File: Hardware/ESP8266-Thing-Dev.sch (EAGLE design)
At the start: 68 parts, among them J1 DNP, Q1 MMBT2222A, Q2 MMBT2222A, U1 AP2112K-3.3V, U2 ESP8266, U3 AT25SF041-SOIC8, U4 FTS31XS-U, Y1 26MHz

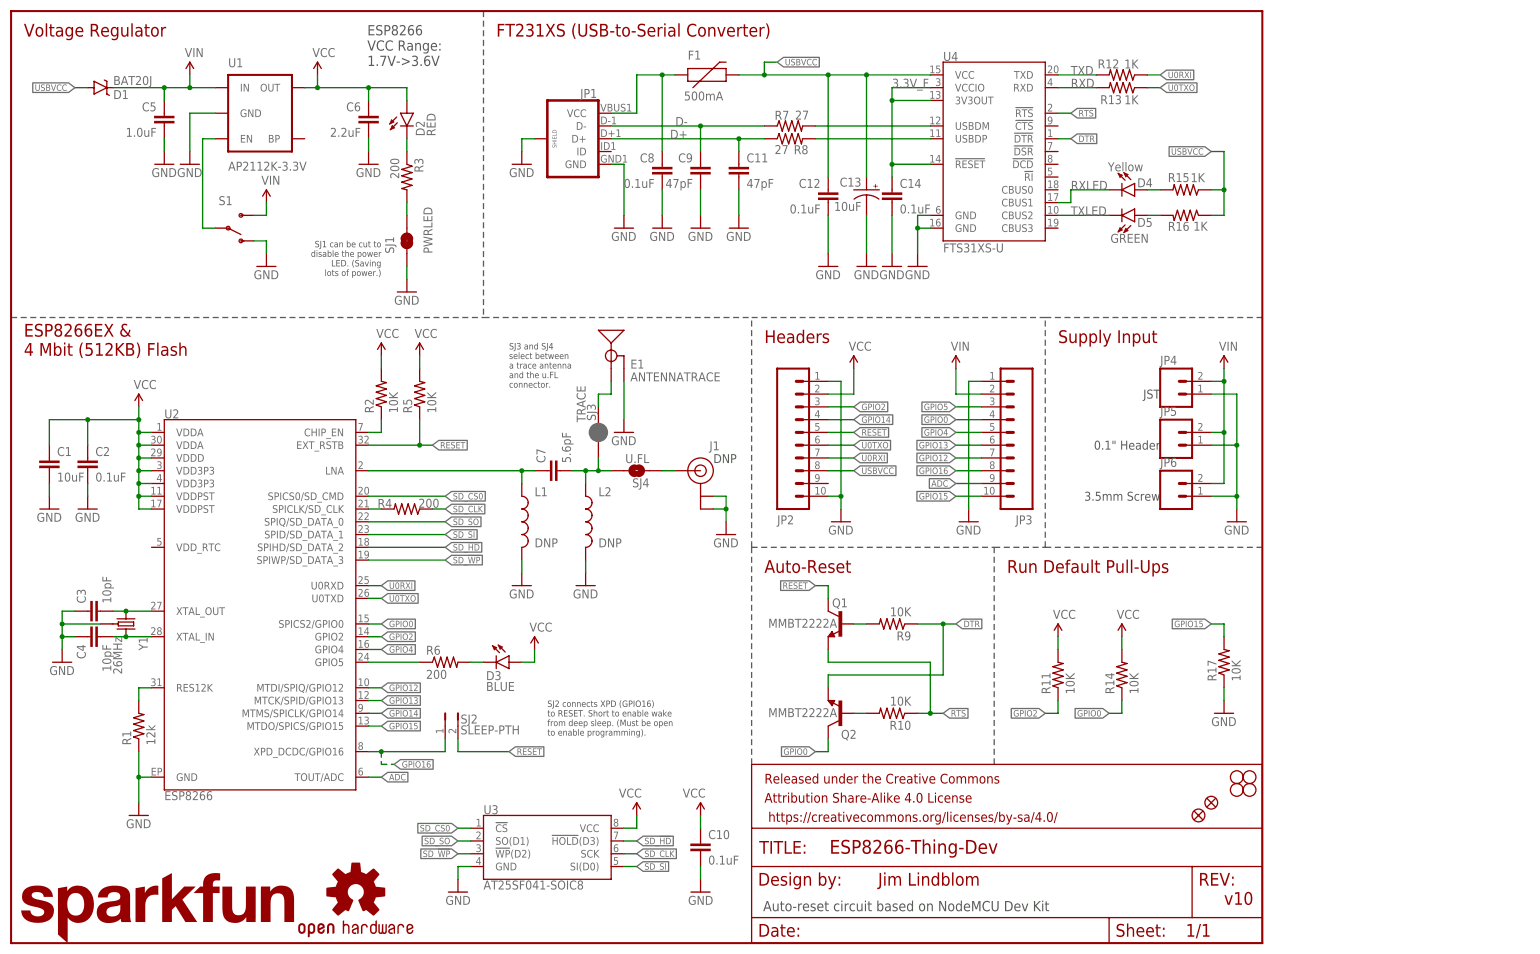
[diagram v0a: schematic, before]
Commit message: Import project and add level shifters in schematic.
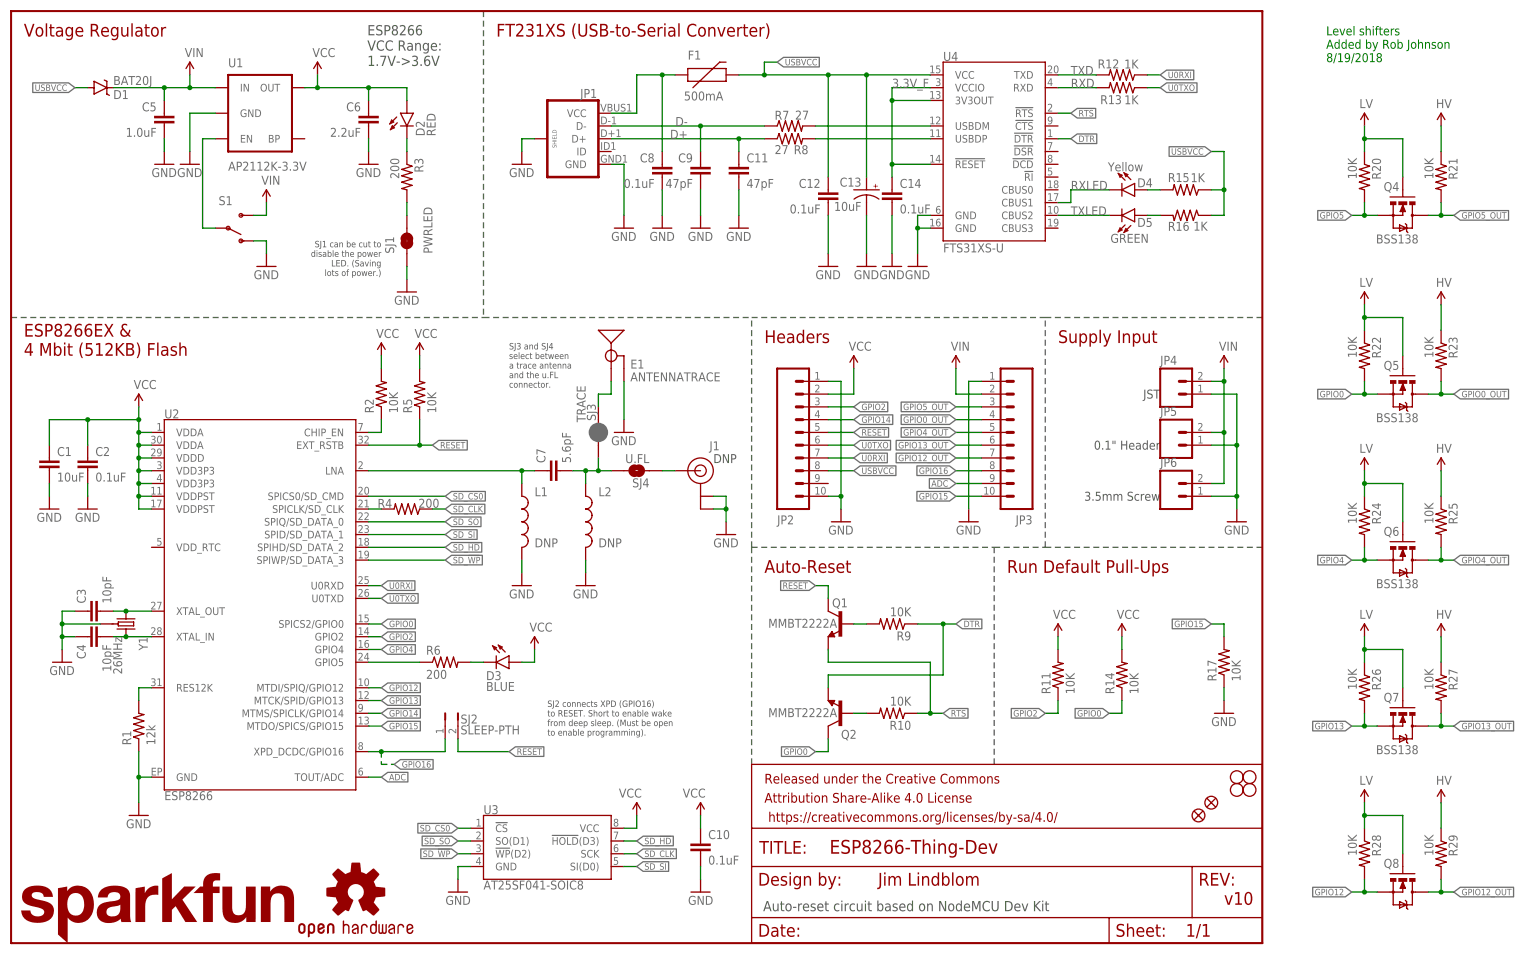
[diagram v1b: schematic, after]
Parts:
- added Q4, Q5, Q6, Q7, Q8: BSS138, SparkFun:MOSFET-NCHANNELSMD
- added R20, R21, R22, R23, R24, R25, R26, R27, R28, R29: 10K, SparkFun:RESISTOR0603-RES
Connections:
- new net GPIO0_OUT: JP3.4, Q5.D, R23.2
- new net GPIO12_OUT: JP3.7, Q8.D, R29.2
- new net GPIO13_OUT: JP3.6, Q7.D, R27.2
- new net GPIO4_OUT: JP3.5, Q6.D, R25.2
- new net GPIO5_OUT: JP3.3, Q4.D, R21.2
- new net HV: R21.1, R23.1, R25.1, R27.1, R29.1
- new net LV: Q5.G, Q6.G, Q7.G, Q8.G, R22.1, R24.1, R26.1, R28.1
- net GPIO0: now also Q5.S, R22.2; no longer JP3.4
- net GPIO12: now also Q8.S, R28.2; no longer JP3.7
- net GPIO13: now also Q7.S, R26.2; no longer JP3.6
- net GPIO4: now also Q6.S, R24.2; no longer JP3.5
- net GPIO5: now also Q4.S, R20.2; no longer JP3.3
- net VCC: now also Q4.G, R20.1
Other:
- note added: "Level shifters Added by Rob Johnson 8/19/2018"

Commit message: Fix Net names for level shifter supply voltages
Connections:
- removed net HV: R21.1, R23.1, R25.1, R27.1, R29.1
- removed net LV: Q5.G, Q6.G, Q7.G, Q8.G, R22.1, R24.1, R26.1, R28.1
- net VCC: now also Q5.G, Q6.G, Q7.G, Q8.G, R22.1, R24.1, R26.1, R28.1
- net VIN: now also R21.1, R23.1, R25.1, R27.1, R29.1

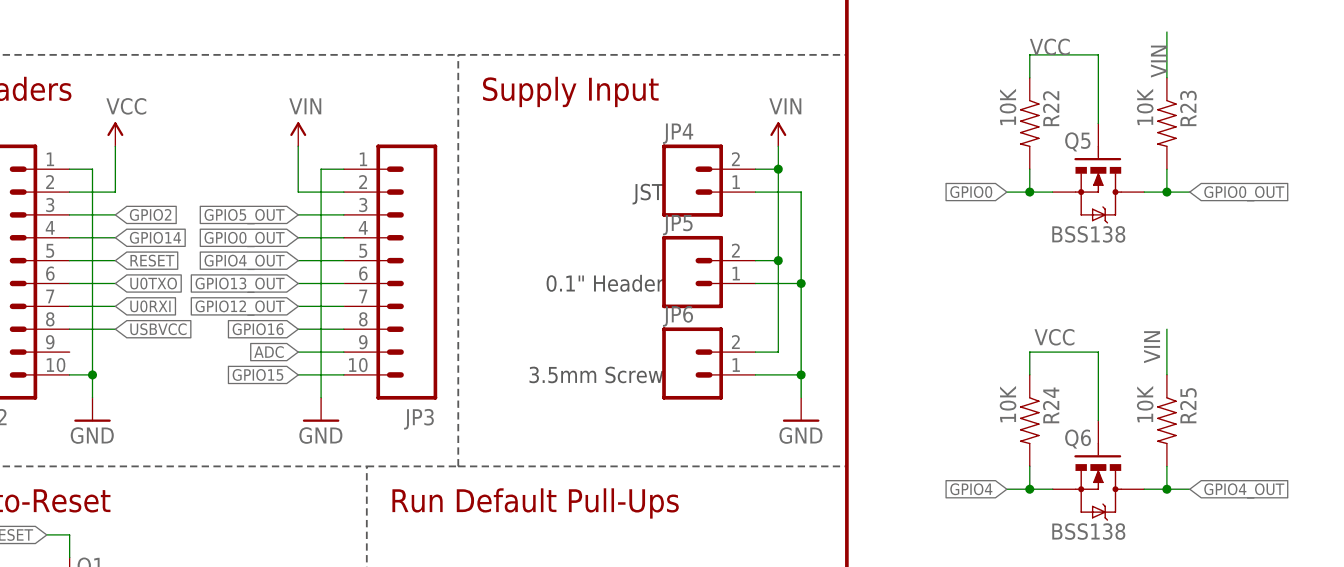
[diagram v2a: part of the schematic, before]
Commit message: Move level shifter on GPIO 0 to GPIO 15.
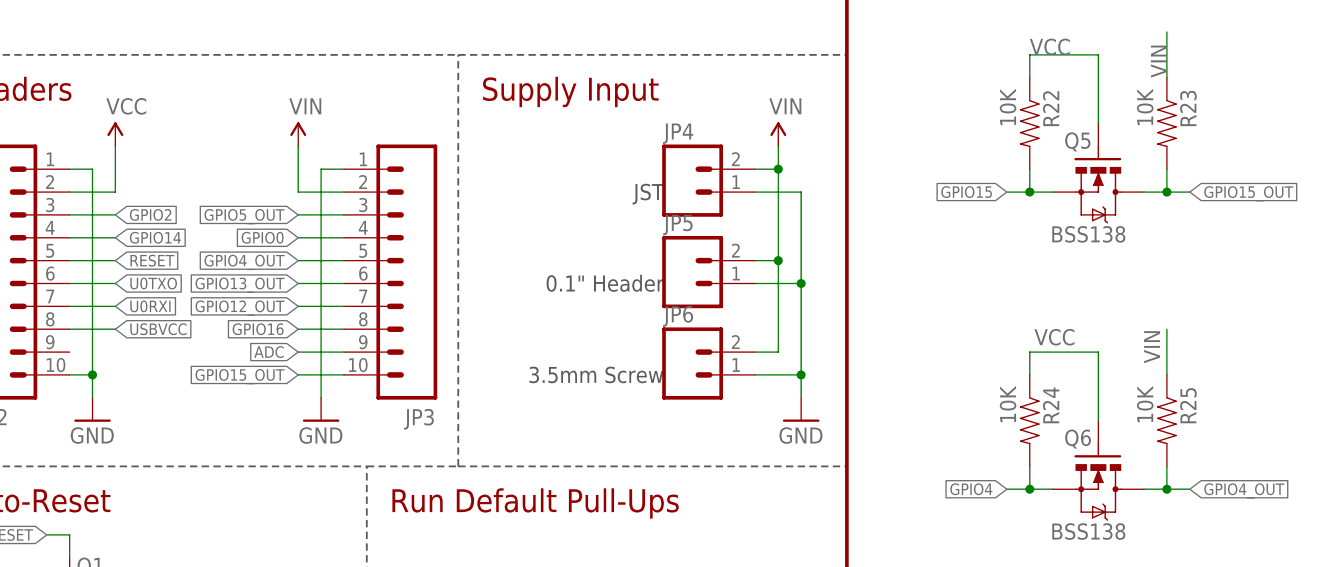
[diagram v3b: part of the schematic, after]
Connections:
- removed net GPIO0_OUT: JP3.4, Q5.D, R23.2
- new net GPIO15_OUT: JP3.10, Q5.D, R23.2
- net GPIO0: now also JP3.4; no longer Q5.S, R22.2
- net GPIO15: now also Q5.S, R22.2; no longer JP3.10
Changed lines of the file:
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@@
 </segment>
 <segment>
-<wire x1="271.78" y1="109.22" x2="269.24" y2="109.22" width="0.1524" layer="91"/>
-<wire x1="269.24" y1="109.22" x2="266.7" y2="109.22" width="0.1524" layer="91"/>
-<wire x1="269.24" y1="111.76" x2="269.24" y2="109.22" width="0.1524" layer="91"/>
-<junction x="269.24" y="109.22"/>
-<pinref part="Q5" gate="G$1" pin="S"/>
-<pinref part="R22" gate="G$1" pin="2"/>
-<label x="266.7" y="109.22" size="1.27" layer="95" rot="R180" xref="yes"/>
+<pinref part="JP3" gate="G$1" pin="4"/>
+<wire x1="193.04" y1="104.14" x2="187.96" y2="104.14" width="0.1524" layer="91"/>
+<label x="187.96" y="104.14" size="1.27" layer="95" rot="R180" xref="yes"/>
 </segment>
 </net>
@@
 </segment>
 <segment>
-<pinref part="JP3" gate="G$1" pin="10"/>
-<wire x1="193.04" y1="88.9" x2="187.96" y2="88.9" width="0.1524" layer="91"/>
-<label x="187.96" y="88.9" size="1.27" layer="95" rot="R180" xref="yes"/>
+<wire x1="271.78" y1="109.22" x2="269.24" y2="109.22" width="0.1524" layer="91"/>
+<wire x1="269.24" y1="109.22" x2="266.7" y2="109.22" width="0.1524" layer="91"/>
+<wire x1="269.24" y1="111.76" x2="269.24" y2="109.22" width="0.1524" layer="91"/>
+<junction x="269.24" y="109.22"/>
+<pinref part="Q5" gate="G$1" pin="S"/>
+<pinref part="R22" gate="G$1" pin="2"/>
+<label x="266.7" y="109.22" size="1.27" layer="95" rot="R180" xref="yes"/>
 </segment>
 </net>
@@
 </segment>
 </net>
-<net name="GPIO0_OUT" class="0">
+<net name="GPIO15_OUT" class="0">
+<segment>
+<pinref part="JP3" gate="G$1" pin="10"/>
+<wire x1="193.04" y1="88.9" x2="187.96" y2="88.9" width="0.1524" layer="91"/>
+<label x="187.96" y="88.9" size="1.27" layer="95" rot="R180" xref="yes"/>
+</segment>
 <segment>
 <wire x1="281.94" y1="109.22" x2="284.48" y2="109.22" width="0.1524" layer="91"/>
@@
 <label x="287.02" y="109.22" size="1.27" layer="95" xref="yes"/>
 </segment>
-<segment>
-<pinref part="JP3" gate="G$1" pin="4"/>
-<wire x1="193.04" y1="104.14" x2="187.96" y2="104.14" width="0.1524" layer="91"/>
-<label x="187.96" y="104.14" size="1.27" layer="95" rot="R180" xref="yes"/>
-</segment>
-</net>
+</net>
